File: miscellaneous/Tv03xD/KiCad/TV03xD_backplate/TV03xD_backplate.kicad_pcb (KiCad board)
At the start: 2 copper layers, 55.5 x 79.8 mm, 5 parts

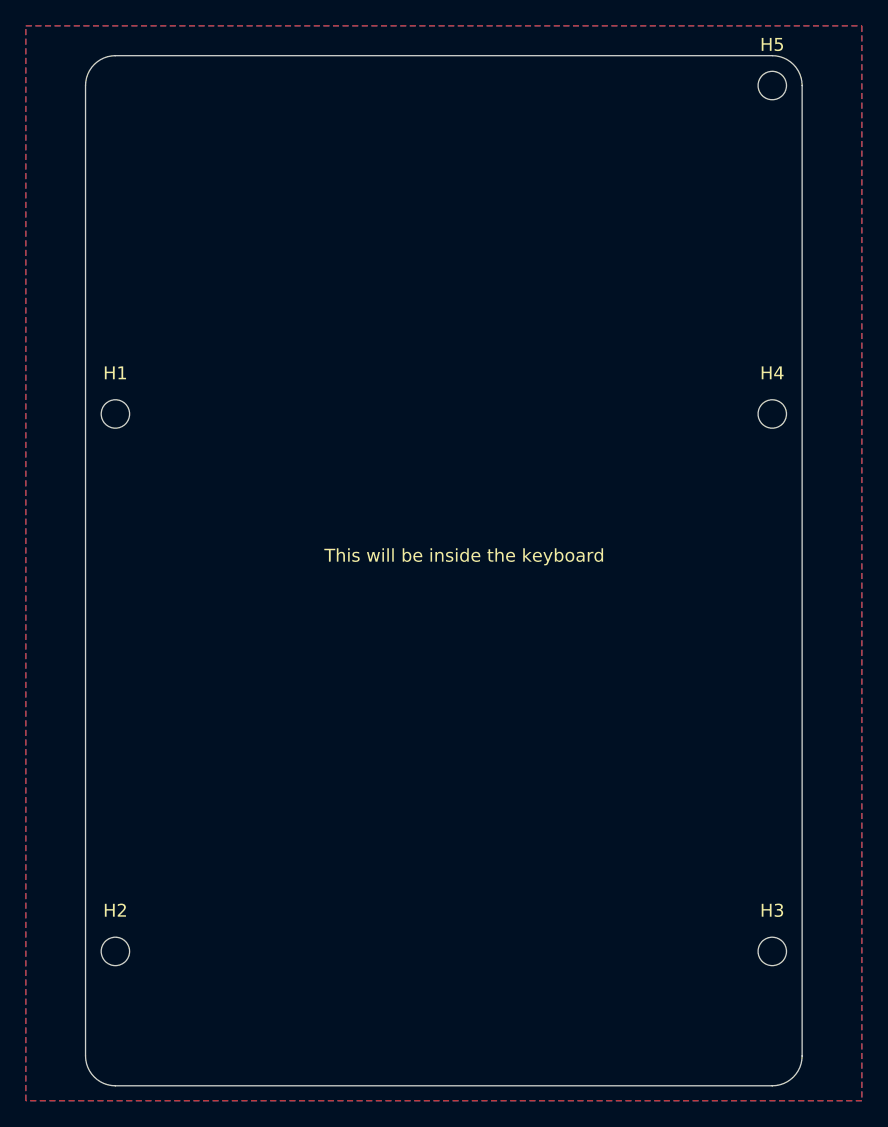
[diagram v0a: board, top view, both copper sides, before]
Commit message: equal in keymap change
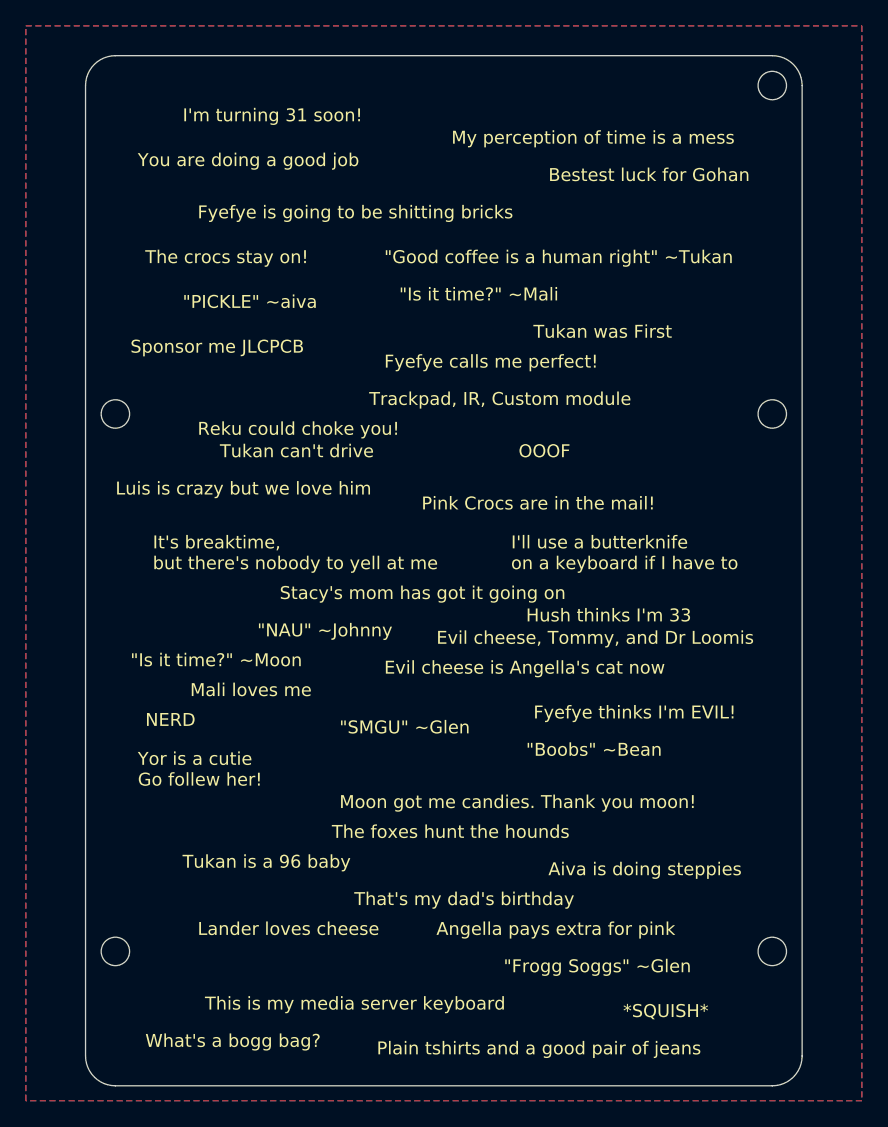
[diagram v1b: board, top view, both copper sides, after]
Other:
- board text added: "*SQUISH*"
- board text added: "Aiva is doing steppies"
- board text added: "Angella pays extra for pink"
- board text added: "Bestest luck for Gohan"
- board text added: "Evil cheese is Angella's cat now"
- board text added: "Evil cheese, Tommy, and Dr Loomis"
- board text added: "Fyefye calls me perfect!"
- board text added: "Fyefye is going to be shitting bricks"
- board text added: "Fyefye thinks I'm EVIL!"
- board text added: "Hush thinks I'm 33"
- board text added: "I'll use a butterknife on a keyboard if I have to"
- board text added: "I'm turning 31 soon!"
- board text added: "It's breaktime, but there's nobody to yell at me"
- board text added: "Lander loves cheese"
- board text added: "Luis is crazy but we love him"
- board text added: "Mali loves me"
- board text added: "Media Server Keyboard Made By Lander03xD"
- board text added: "Moon got me candies. Thank you moon!"
- board text added: "My perception of time is a mess"
- board text added: "NERD"
- board text added: "OOOF"
- board text added: "Pink Crocs are in the mail!"
- board text added: "Plain tshirts and a good pair of jeans"
- board text added: "Reku could choke you!"
- board text added: "Sponsor me JLCPCB"
- board text added: "Stacy's mom has got it going on"
- board text added: "That's my dad's birthday"
- board text added: "The crocs stay on!"
- board text added: "The foxes hunt the hounds"
- board text added: "This is my media server keyboard"
- board text added: "Trackpad, IR, Custom module"
- board text added: "Tukan can't drive"
- board text added: "Tukan is a 96 baby"
- board text added: "Tukan was First"
- board text added: "What's a bogg bag?"
- board text added: "Yor is a cutie Go follew her!"
- board text added: "You are doing a good job"
- board text added: "{dblquote}Boobs{dblquote} ~Bean"
- board text added: "{dblquote}Frogg Soggs{dblquote} ~Glen"
- board text added: "{dblquote}Good coffee is a human right{dblquote} ~Tukan"
- board text added: "{dblquote}Is it time?{dblquote} ~Mali"
- board text added: "{dblquote}Is it time?{dblquote} ~Moon"
- board text added: "{dblquote}NAU{dblquote} ~Johnny"
- board text added: "{dblquote}PICKLE{dblquote} ~aiva"
- board text added: "{dblquote}SMGU{dblquote} ~Glen"
- board text removed: "This is visible"
- board text removed: "This will be inside the keyboard"
